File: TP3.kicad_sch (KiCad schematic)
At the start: 48 parts

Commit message: Puse un pin doble para Chf
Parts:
- removed C_HF1, C_HF2: (no value), Connector_PinSocket_1.27mm:PinSocket_1x01_P1.27mm_Vertical, symbol Connector:TestPoint
- added C_HF1: Conn_01x02, Connector_PinSocket_2.54mm:PinSocket_1x02_P2.54mm_Vertical, symbol Connector_Generic:Conn_01x02
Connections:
- net at C_o1.1, M_2.3 (D), R_D2.2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: now also C_HF1.1 (Pin_1)
- net at I_Rga1.1 (A), I_Rgb1.1 (A), Id_M1.1 (A)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: now also C_HF1.2 (Pin_2)
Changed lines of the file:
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@@
 	)
 	(junction
-		(at 162.56 161.29)
+		(at 166.37 49.53)
 		(diameter 0)
 		(color 0 0 0 0)
 	)
 	(junction
-		(at 166.37 49.53)
+		(at 162.56 161.29)
 		(diameter 0)
 		(color 0 0 0 0)
@@
 	(wire
 		(pts
-			(xy 144.78 49.53) (xy 166.37 49.53)
-		)
-		(stroke
-			(width 0)
-			(type default)
-		)
-	)
-	(wire
-		(pts
 			(xy 92.71 147.32) (xy 92.71 151.13)
 		)
@@
 	(wire
 		(pts
+			(xy 166.37 49.53) (xy 166.37 63.5)
+		)
+		(stroke
+			(width 0)
+			(type default)
+		)
+	)
+	(wire
+		(pts
 			(xy 120.65 87.63) (xy 124.46 87.63)
 		)
@@
 	(wire
 		(pts
-			(xy 166.37 49.53) (xy 166.37 59.69)
-		)
-		(stroke
-			(width 0)
-			(type default)
-		)
-	)
-	(wire
-		(pts
 			(xy 190.5 148.59) (xy 190.5 152.4)
 		)
@@
 	(wire
 		(pts
+			(xy 166.37 66.04) (xy 166.37 81.28)
+		)
+		(stroke
+			(width 0)
+			(type default)
+		)
+	)
+	(wire
+		(pts
 			(xy 186.69 81.28) (xy 193.04 81.28)
 		)
@@
 	(wire
 		(pts
-			(xy 182.88 148.59) (xy 182.88 143.51)
+			(xy 144.78 49.53) (xy 166.37 49.53)
 		)
 		(stroke
@@
 	(wire
 		(pts
-			(xy 144.78 41.91) (xy 144.78 49.53)
+			(xy 182.88 148.59) (xy 182.88 143.51)
 		)
 		(stroke
@@
 	(wire
 		(pts
-			(xy 166.37 67.31) (xy 166.37 81.28)
+			(xy 144.78 41.91) (xy 144.78 49.53)
 		)
 		(stroke
@@
 	)
 	(symbol
-		(lib_id "Connector:TestPoint")
-		(at 166.37 67.31 270)
-		(unit 1)
-		(body_style 1)
-		(exclude_from_sim no)
-		(in_bom yes)
-		(on_board yes)
-		(in_pos_files yes)
-		(dnp no)
-		(property "Reference" "C_HF2"
-			(at 171.196 67.31 90)
-			(show_name no)
-			(do_not_autoplace no)
-			(effects
-				(font
-					(size 1.27 1.27)
-				)
-				(justify left)
-			)
-		)
-		(property "Value" ""
-			(at 172.212 62.23 0)
-			(show_name no)
-			(do_not_autoplace no)
-			(effects
-				(font
-					(size 1.27 1.27)
-				)
-				(justify left)
-			)
-		)
-		(property "Footprint" "Connector_PinSocket_1.27mm:PinSocket_1x01_P1.27mm_Vertical"
-			(at 166.37 72.39 0)
-			(hide yes)
-			(show_name no)
-			(do_not_autoplace no)
-			(effects
-				(font
-					(size 1.27 1.27)
-				)
-			)
-		)
-		(property "Datasheet" ""
-			(at 166.37 72.39 0)
-			(hide yes)
-			(show_name no)
-			(do_not_autoplace no)
-			(effects
-				(font
-					(size 1.27 1.27)
-				)
-			)
-		)
-		(property "Description" "test point"
-			(at 166.37 67.31 0)
-			(hide yes)
-			(show_name no)
-			(do_not_autoplace no)
-			(effects
-				(font
-					(size 1.27 1.27)
-				)
-			)
-		)
-		(pin "1"
-		)
-		(instances
-			(project "TP3"
-				(path "/610a7397-f790-40ce-8984-3eafd1c20c20"
-					(reference "C_HF2")
-					(unit 1)
-				)
-			)
-		)
-	)
-	(symbol
 		(lib_id "power:GND")
 		(at 175.26 39.37 0)
@@
 	)
 	(symbol
-		(lib_id "Connector:TestPoint")
-		(at 166.37 59.69 90)
-		(unit 1)
-		(body_style 1)
-		(exclude_from_sim no)
-		(in_bom yes)
-		(on_board yes)
-		(in_pos_files yes)
-		(dnp no)
-		(property "Reference" "C_HF1"
-			(at 161.544 59.69 90)
-			(show_name no)
-			(do_not_autoplace no)
-			(effects
-				(font
-					(size 1.27 1.27)
-				)
-				(justify left)
-			)
-		)
-		(property "Value" ""
-			(at 160.528 64.77 0)
-			(show_name no)
-			(do_not_autoplace no)
-			(effects
-				(font
-					(size 1.27 1.27)
-				)
-				(justify left)
-			)
-		)
-		(property "Footprint" "Connector_PinSocket_1.27mm:PinSocket_1x01_P1.27mm_Vertical"
-			(at 166.37 54.61 0)
-			(hide yes)
-			(show_name no)
-			(do_not_autoplace no)
-			(effects
-				(font
-					(size 1.27 1.27)
-				)
-			)
-		)
-		(property "Datasheet" ""
-			(at 166.37 54.61 0)
-			(hide yes)
-			(show_name no)
-			(do_not_autoplace no)
-			(effects
-				(font
-					(size 1.27 1.27)
-				)
-			)
-		)
-		(property "Description" "test point"
-			(at 166.37 59.69 0)
-			(hide yes)
-			(show_name no)
-			(do_not_autoplace no)
-			(effects
-				(font
-					(size 1.27 1.27)
-				)
-			)
-		)
-		(pin "1"
-		)
-		(instances
-			(project "TP3"
-				(path "/610a7397-f790-40ce-8984-3eafd1c20c20"
-					(reference "C_HF1")
-					(unit 1)
-				)
-			)
-		)
-	)
-	(symbol
 		(lib_id "Device:R_US")
 		(at 222.25 91.44 0)
@@
 	)
 	(symbol
+		(lib_id "Connector_Generic:Conn_01x02")
+		(at 161.29 66.04 180)
+		(unit 1)
+		(body_style 1)
+		(exclude_from_sim no)
+		(in_bom yes)
+		(on_board yes)
+		(in_pos_files yes)
+		(dnp no)
+		(fields_autoplaced yes)
+		(property "Reference" "C_HF1"
+			(at 161.29 59.69 0)
+			(show_name no)
+			(do_not_autoplace no)
+			(effects
+				(font
+					(size 1.27 1.27)
+				)
+			)
+		)
+		(property "Value" "Conn_01x02"
+			(at 161.29 59.69 0)
+			(hide yes)
+			(show_name no)
+			(do_not_autoplace no)
+			(effects
+				(font
+					(size 1.27 1.27)
+				)
+			)
+		)
+		(property "Footprint" "Connector_PinSocket_2.54mm:PinSocket_1x02_P2.54mm_Vertical"
+			(at 161.29 66.04 0)
+			(hide yes)
+			(show_name no)
+			(do_not_autoplace no)
+			(effects
+				(font
+					(size 1.27 1.27)
+				)
+			)
+		)
+		(property "Datasheet" ""
+			(at 161.29 66.04 0)
+			(hide yes)
+			(show_name no)
+			(do_not_autoplace no)
+			(effects
+				(font
+					(size 1.27 1.27)
+				)
+			)
+		)
+		(property "Description" "Generic connector, single row, 01x02, script generated (kicad-library-utils/schlib/autogen/connector/)"
+			(at 161.29 66.04 0)
+			(hide yes)
+			(show_name no)
+			(do_not_autoplace no)
+			(effects
+				(font
+					(size 1.27 1.27)
+				)
+			)
+		)
+		(pin "2"
+		)
+		(pin "1"
+		)
+		(instances
+			(project "TP3"
+				(path "/610a7397-f790-40ce-8984-3eafd1c20c20"
+					(reference "C_HF1")
+					(unit 1)
+				)
+			)
+		)
+	)
+	(symbol
 		(lib_id "Jumper:Jumper_2_Bridged")
 		(at 243.84 54.61 270)
@@
 		(dnp no)
 		(property "Reference" "GND1"
-			(at 163.068 31.242 0)
+			(at 162.306 31.75 0)
 			(show_name no)
 			(do_not_autoplace no)
@@
 		)
 		(property "Value" "TestPoint"
-			(at 160.02 33.528 0)
+			(at 160.02 29.718 0)
 			(show_name no)
 			(do_not_autoplace no)

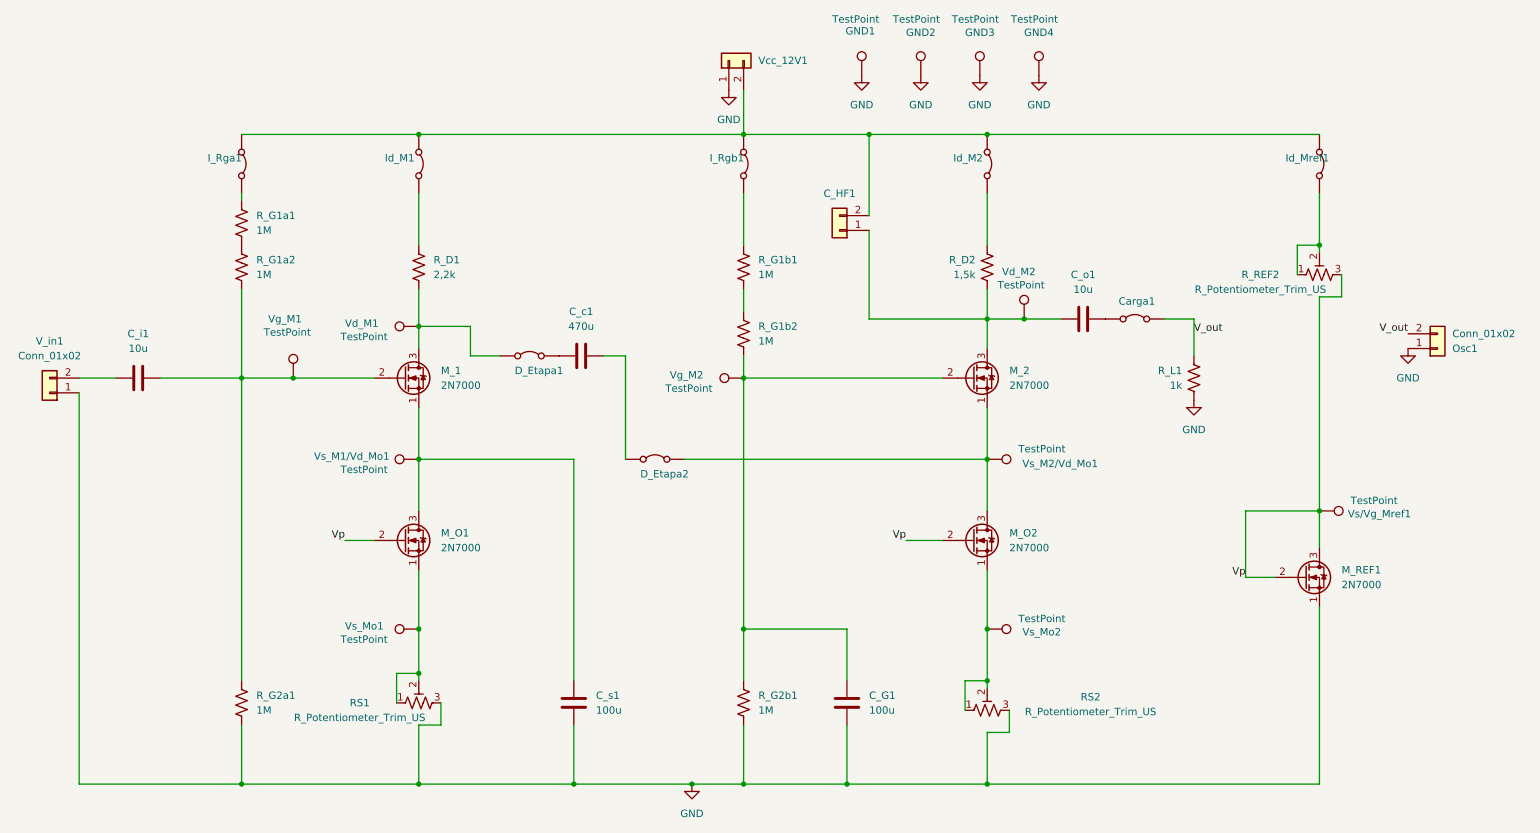
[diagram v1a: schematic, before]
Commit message: Placa hecha, se usó una huella para C_c1 con las patas más separadas para hacer pasar la pista de la referencia
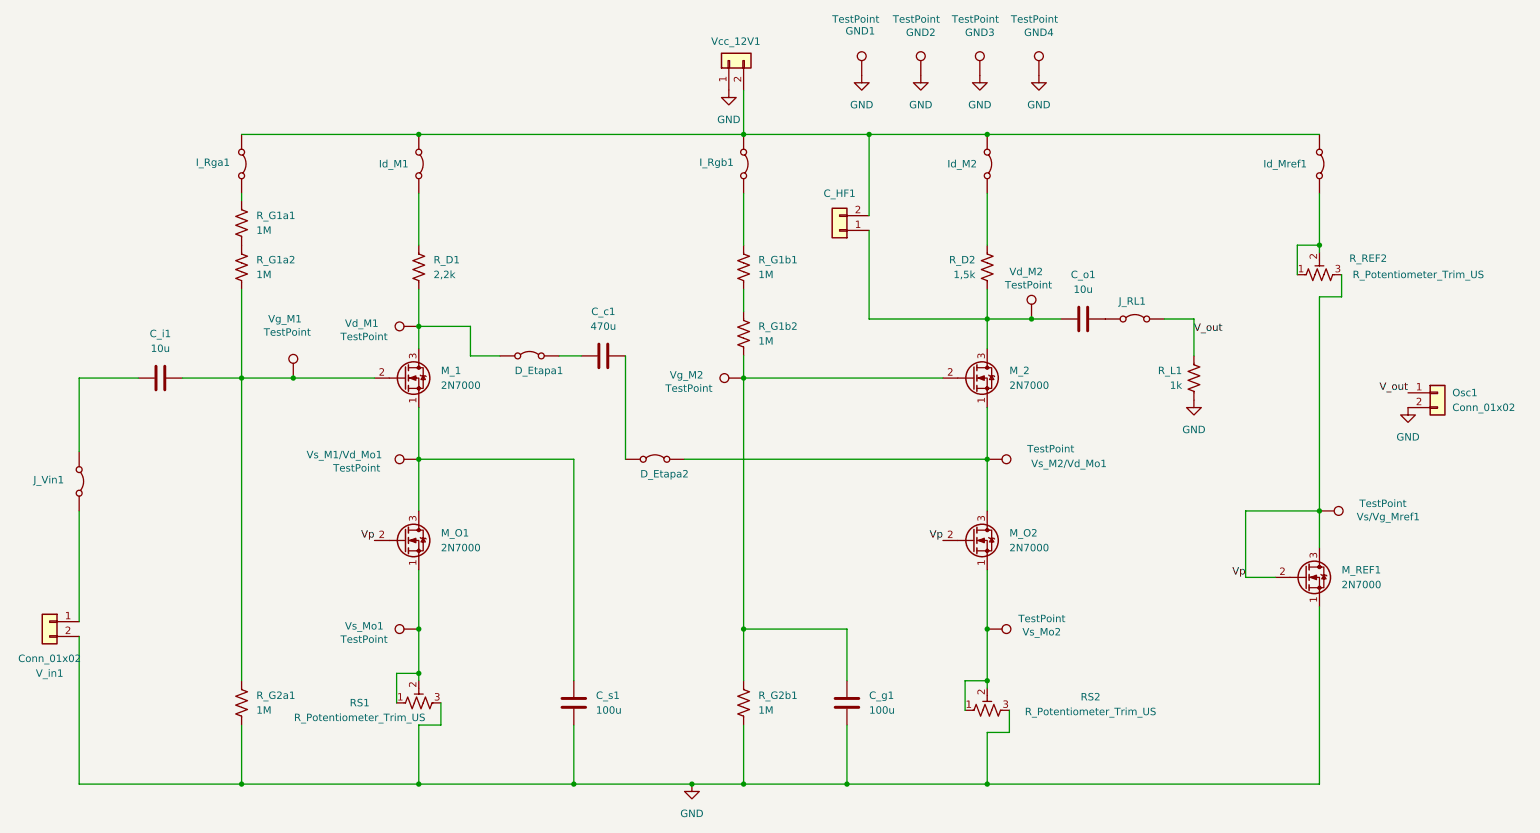
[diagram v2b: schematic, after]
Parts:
- added J_Vin1: Jumper_2_Bridged, Connector_PinHeader_2.54mm:PinHeader_1x02_P2.54mm_Vertical, symbol Jumper:Jumper_2_Bridged
- C_c1: footprint Capacitor_THT:CP_Radial_D10.0mm_P3.80mm -> Capacitor_THT:CP_Radial_D10.0mm_P7.50mm
- renumbered C_G1 to C_g1, Carga1 to J_RL1
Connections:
- net GND: now also Osc1.2 (Pin_2), V_in1.2 (Pin_2); no longer Osc1.1 (Pin_1), V_in1.1 (Pin_1)
- net V_out: now also Osc1.1 (Pin_1); no longer Osc1.2 (Pin_2)
- net at C_i1.1: now also J_Vin1.1 (A); no longer V_in1.2 (Pin_2)
- new net: J_Vin1.2 (B), V_in1.1 (Pin_1)
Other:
- moved on the sheet: C_c1, C_i1, Osc1, V_in1, Vd_M2
